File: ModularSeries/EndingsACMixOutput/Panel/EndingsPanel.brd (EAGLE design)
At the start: 50.5 x 128.5 mm, 14 parts

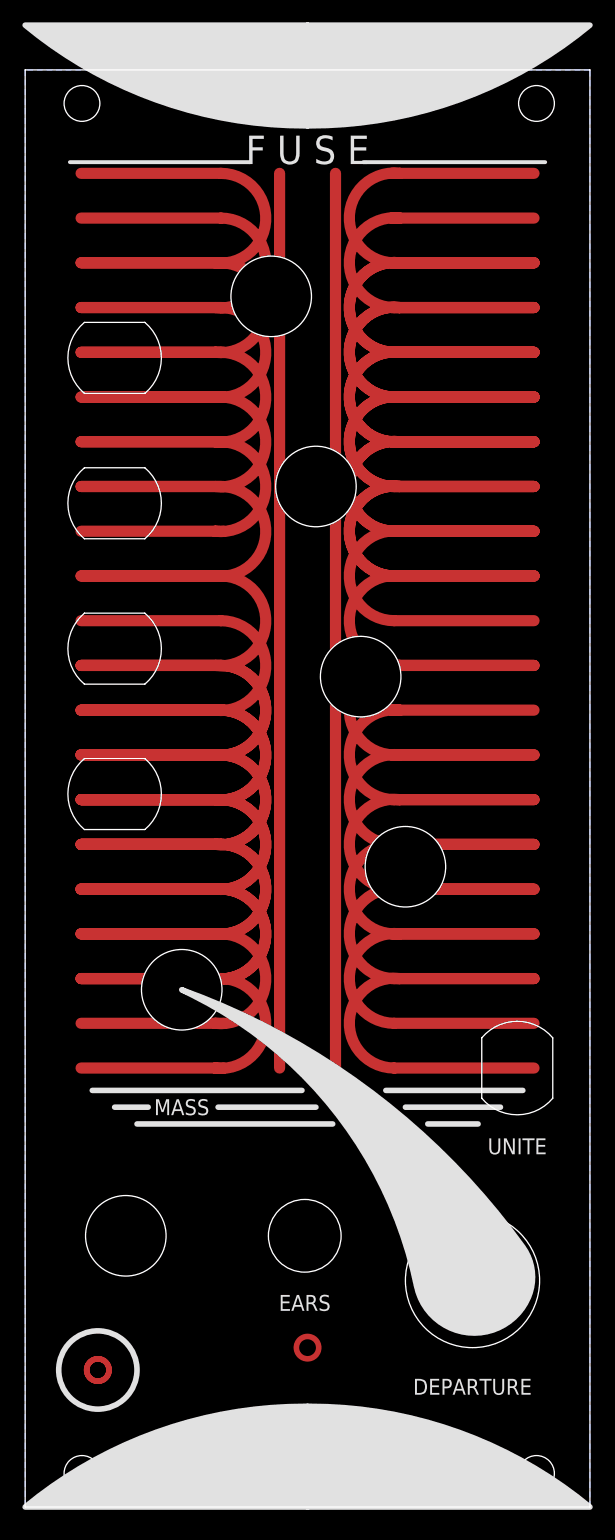
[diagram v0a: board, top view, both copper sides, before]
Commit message: Layout and schematic renders for LHP added
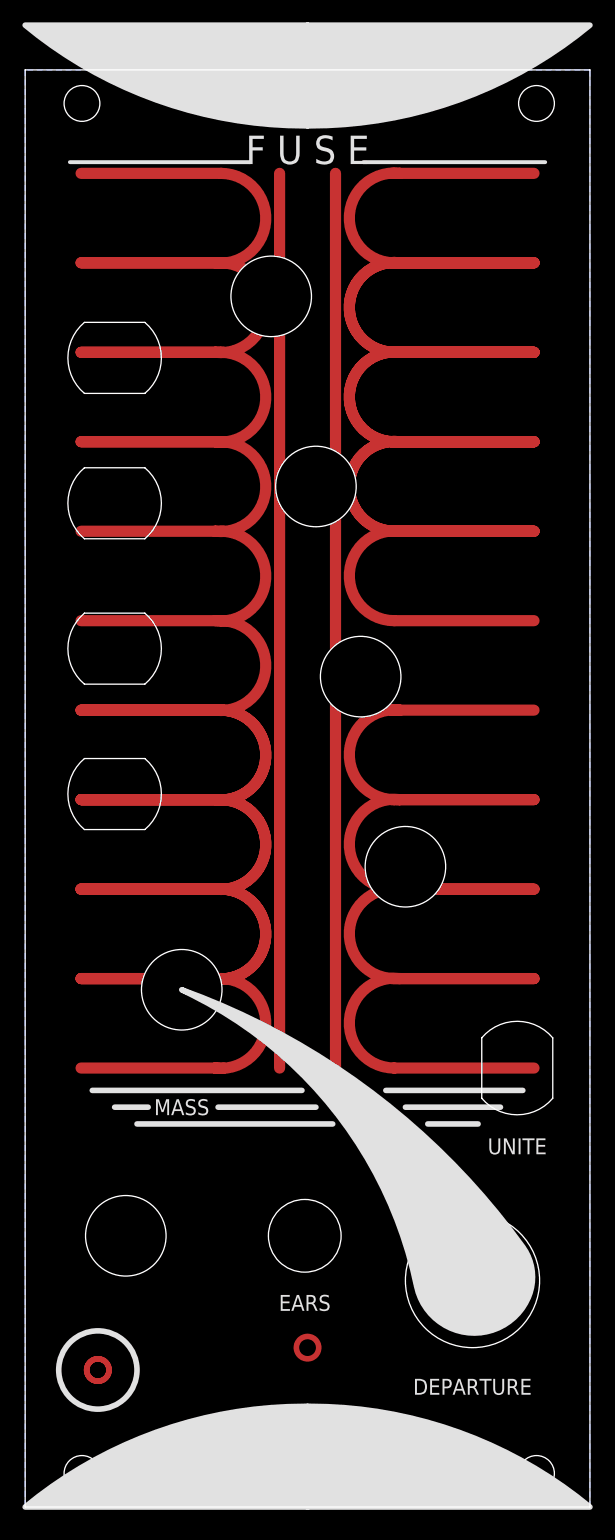
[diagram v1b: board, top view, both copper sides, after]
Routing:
- net S$91: track 12.5 -> 0.00 mm
- net S$83: track 12.5 -> 0.00 mm
- net S$75: track 12.5 -> 0.00 mm
- net S$7: track 12.5 -> 0.00 mm
- net S$67: track 12.5 -> 0.00 mm
- net S$59: track 12.5 -> 0.00 mm
- net S$51: track 12.5 -> 0.00 mm
- net S$43: track 12.5 -> 0.00 mm
- net S$35: track 12.5 -> 0.00 mm
- net S$31: track 12.5 -> 0.00 mm
- net S$23: track 12.5 -> 0.00 mm
- net S$187: track 12.5 -> 0.00 mm
- net S$179: track 12.5 -> 0.00 mm
- net S$171: track 12.5 -> 0.00 mm
- net S$163: track 12.5 -> 0.00 mm
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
